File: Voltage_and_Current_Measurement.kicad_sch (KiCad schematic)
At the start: 0 parts

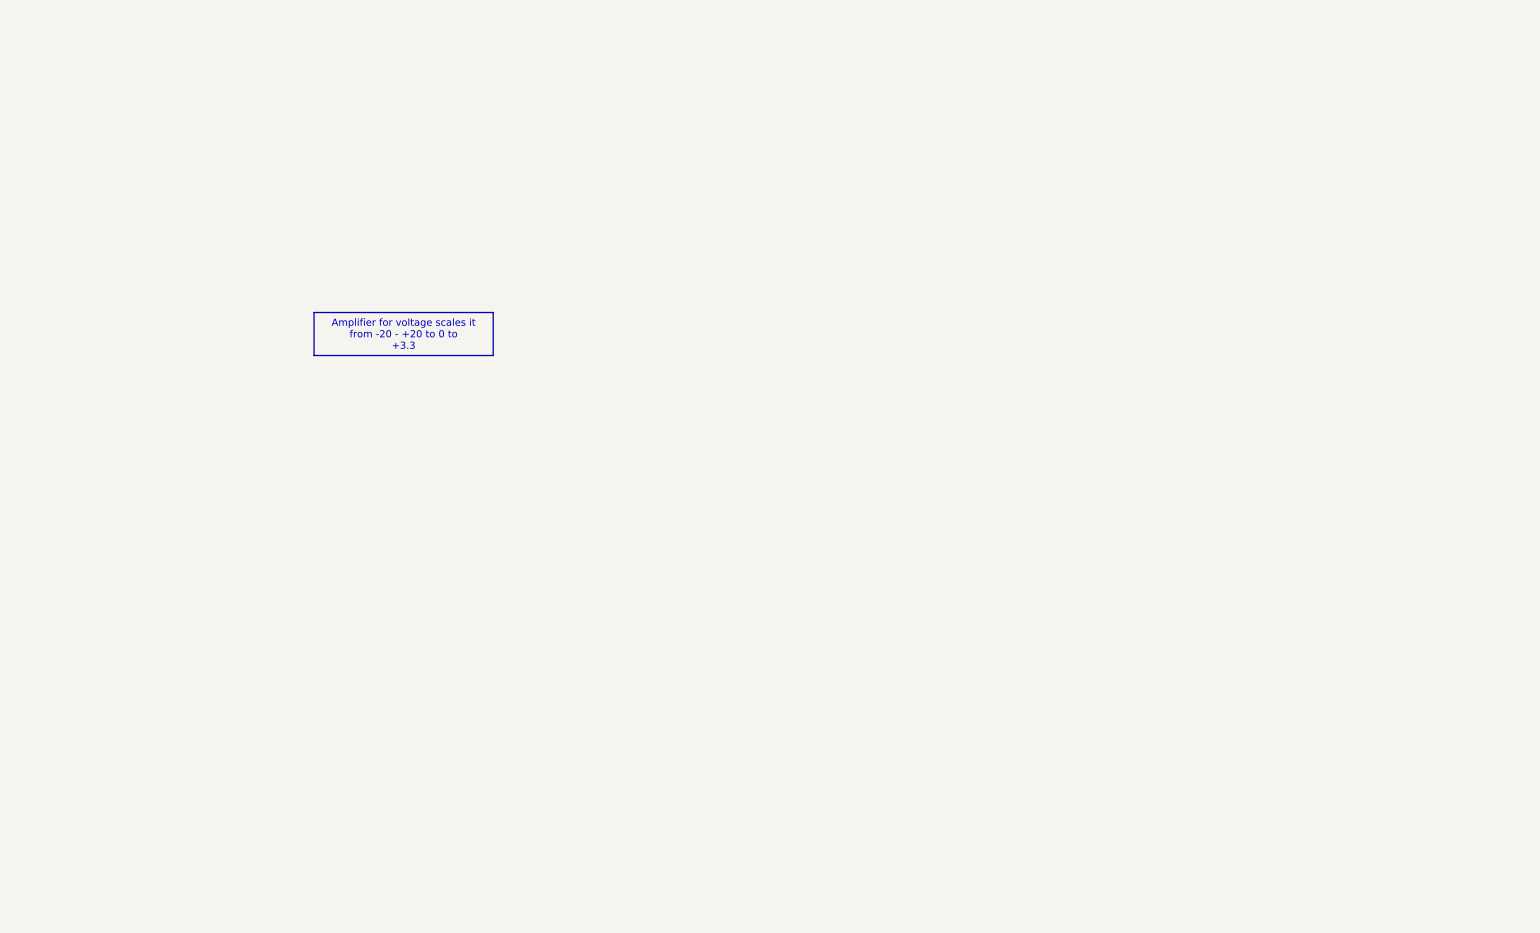
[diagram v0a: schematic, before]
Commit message: added voltage measurement and current measurement
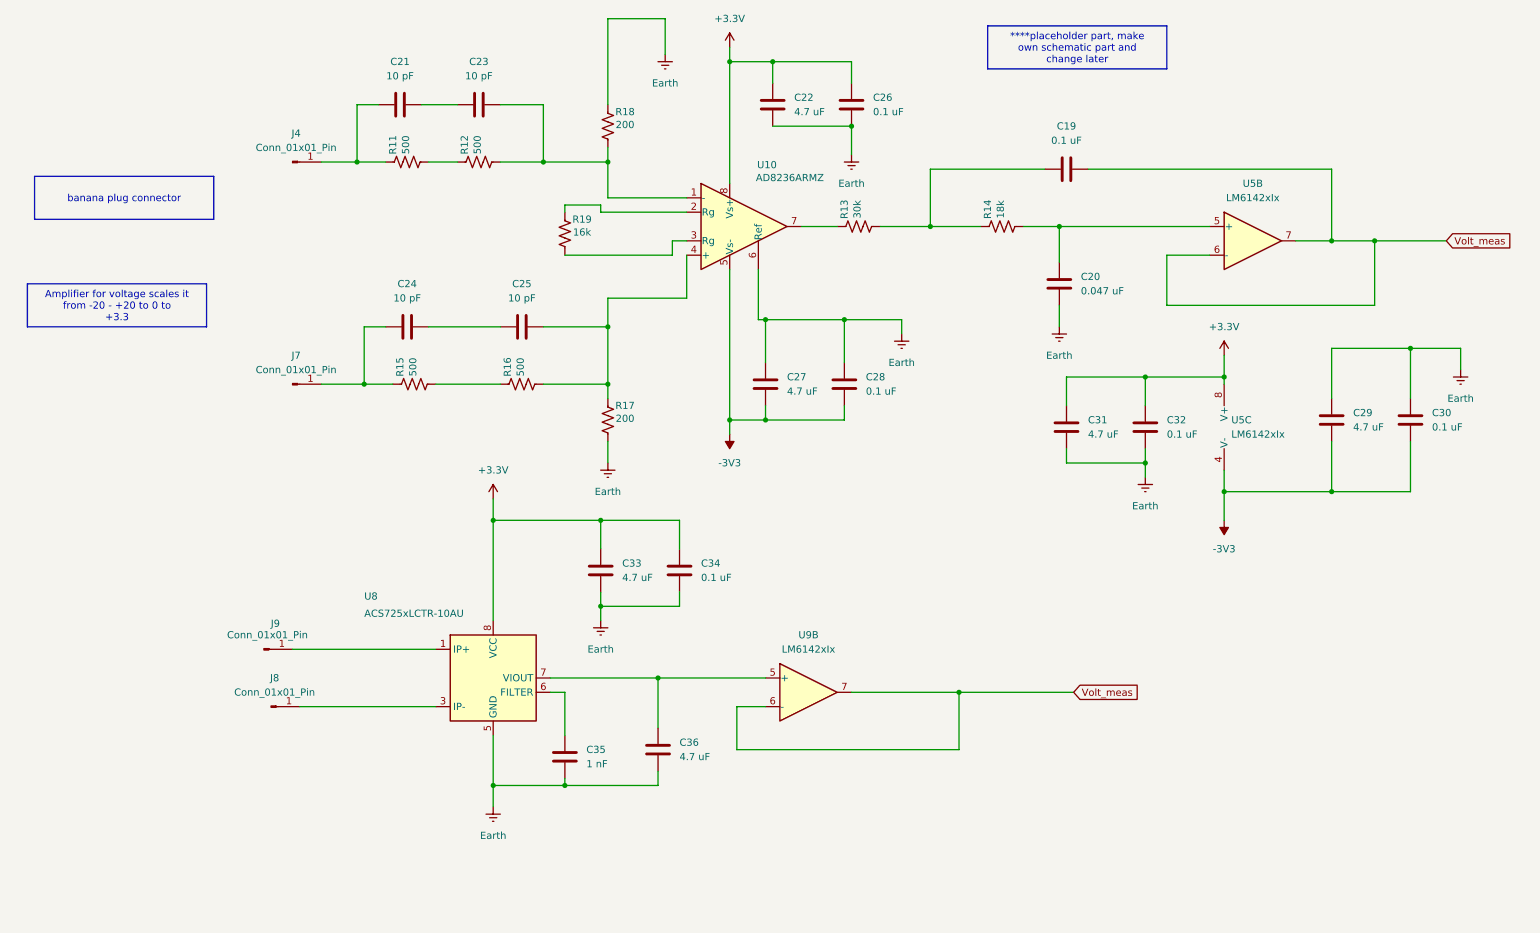
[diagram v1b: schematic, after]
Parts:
- added C19, C26, C28, C30, C32, C34: 0.1 uF, symbol Device:C
- added C20: 0.047 uF, symbol Device:C
- added C21, C23, C24, C25: 10 pF, symbol Device:C
- added C22, C27, C29, C31, C33, C36: 4.7 uF, symbol Device:C
- added C35: 1 nF, symbol Device:C
- added J4, J7, J8, J9: Conn_01x01_Pin, symbol Connector:Conn_01x01_Pin
- added R11, R12, R15, R16: 500, symbol Device:R_US
- added R13: 30k, symbol Device:R_US
- added R14: 18k, symbol Device:R_US
- added R17, R18: 200, symbol Device:R_US
- added R19: 16k, symbol Device:R_US
- added U10: AD8236ARMZ, symbol Amplifier_Instrumentation:AD8236ARMZ
- added U5, U9: LM6142xIx, symbol Amplifier_Operational:LM6142xIx
- added U8: ACS725xLCTR-10AU, Package_SO:SOIC-8_3.9x4.9mm_P1.27mm, symbol Sensor_Current:ACS725xLCTR-10AU
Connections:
- new net: C21.2, C23.1
- new net: C23.2, R12.2, R18.2, U10.1 (-)
- new net: C20.2, R14.2, U5.5 (+)
- new net: R13.1, U10.7
- new net: C19.1, R13.2, R14.1
- new net: C35.2, U8.6 (FILTER)
- new net: C21.1, J4.1 (Pin_1), R11.1
- new net: J9.1 (Pin_1), U8.1 (IP+), U8.2 (IP+)
- new net: J8.1 (Pin_1), U8.3 (IP-), U8.4 (IP-)
- new net: C36.2, U8.7 (VIOUT), U9.5 (+)
- new net: R11.2, R12.1
- new net: R19.1, U10.2 (Rg)
- new net: R19.2, U10.3 (Rg)
- new net: C24.2, C25.1
- new net: C25.2, R16.2, R17.1, U10.4 (+)
- new net: C24.1, J7.1 (Pin_1), R15.1
- new net: R15.2, R16.1
- new net +3.3V: C22.2, C26.2, C31.2, C32.2, C33.2, C34.2, U10.8 (Vs+), U5.8 (V+), U8.8 (VCC)
- new net -3V3: C27.1, C28.1, C29.1, C30.1, U10.5 (Vs-), U5.4 (V-)
- new net Earth: C20.1, C22.1, C26.1, C27.2, C28.2, C29.2, C30.2, C31.1, C32.1, C33.1, C34.1, C35.1, C36.1, R17.2, R18.1, U10.6 (Ref), U8.5 (GND)
- new net Volt_meas: C19.2, U5.6 (-), U5.7, U9.6 (-), U9.7

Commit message: updated schematics added the stm cube project file
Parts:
- removed U5, U9: LM6142xIx, symbol Amplifier_Operational:LM6142xIx
- added U12: LMV324, symbol Amplifier_Operational:LMV324
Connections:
- net +3.3V: now also U12.4 (V+)
- net -3V3: now also U12.11 (V-)
- net Volt_meas: now also U12.1, U12.2 (-)
- net at C20.2, R14.2: now also U12.3 (+)
- net at C36.2, U8.7 (VIOUT): now also U12.5 (+)
- new net Curr_Meas: U12.6 (-), U12.7
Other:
- moved on the sheet: C33, C34, C35, C36, J8, J9, U8

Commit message: changes to schematic and PCB
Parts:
- C19, C20, C21, C22, C23, C24, C25, C26, C27, C28, C29, C30, C31, C32, C33, C34, C35, C36: footprint (none) -> Capacitor_SMD:C_0805_2012Metric
- J4, J7, J8, J9: footprint (none) -> Connector:Banana_Jack_1Pin
- R11, R12, R13, R14, R15, R16, R17, R18, R19: footprint (none) -> Resistor_SMD:R_0805_2012Metric
- U10: footprint (none) -> Package_SO:MSOP-8_3x3mm_P0.65mm
- U12: footprint (none) -> STM32_Play_Board:SOIC-14_3.9x8.7mm_P1.27mm_STM32_Play
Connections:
- net Curr_Meas renamed Curr_meas
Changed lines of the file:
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@@
 		)
 	)
-	(global_label "Curr_Meas"
-		(shape input)
+	(hierarchical_label "Curr_meas"
+		(shape passive)
 		(at 177.8 148.59 0)
 		(fields_autoplaced yes)
@@
 			(justify left)
 		)
-		(property "Intersheetrefs" "${INTERSHEET_REFS}"
-			(at 190.4613 148.59 0)
-			(effects
-				(font
-					(size 1.27 1.27)
-				)
-				(justify left)
-				(hide yes)
-			)
-		)
 	)
-	(global_label "Volt_meas"
-		(shape input)
+	(hierarchical_label "Volt_meas"
+		(shape passive)
 		(at 266.7 54.61 0)
 		(fields_autoplaced yes)
@@
 			(justify left)
 		)
-		(property "Intersheetrefs" "${INTERSHEET_REFS}"
-			(at 279.2403 54.61 0)
-			(effects
-				(font
-					(size 1.27 1.27)
-				)
-				(justify left)
-				(hide yes)
-			)
-		)
 	)
 	(symbol
@@
 			)
 		)
-		(property "Footprint" ""
+		(property "Footprint" "Capacitor_SMD:C_0805_2012Metric"
 			(at 99.06 29.5148 0)
 			(effects
@@
 			)
 		)
-		(property "Footprint" ""
+		(property "Footprint" "Capacitor_SMD:C_0805_2012Metric"
 			(at 197.1548 58.42 0)
 			(effects
@@
 			)
 		)
-		(property "Footprint" ""
+		(property "Footprint" "Resistor_SMD:R_0805_2012Metric"
 			(at 162.814 51.054 90)
 			(effects
@@
 			)
 		)
-		(property "Footprint" ""
+		(property "Footprint" "Capacitor_SMD:C_0805_2012Metric"
 			(at 86.6648 156.21 0)
 			(effects
@@
 			)
 		)
-		(property "Footprint" ""
+		(property "Footprint" "Capacitor_SMD:C_0805_2012Metric"
 			(at 212.3948 83.82 0)
 			(effects
@@
 			)
 		)
-		(property "Footprint" ""
+		(property "Footprint" "STM32_Play_Board:SOIC-14_3.9x8.7mm_P1.27mm_STM32_Play"
 			(at 231.14 52.07 0)
 			(effects
@@
 			)
 		)
-		(property "Footprint" ""
+		(property "Footprint" "Resistor_SMD:R_0805_2012Metric"
 			(at 119.126 34.544 90)
 			(effects
@@
 			)
 		)
-		(property "Footprint" ""
+		(property "Footprint" "Connector:Banana_Jack_1Pin"
 			(at 62.23 40.64 0)
 			(effects
@@
 			)
 		)
-		(property "Footprint" ""
+		(property "Footprint" "Capacitor_SMD:C_0805_2012Metric"
 			(at 259.3848 82.55 0)
 			(effects
@@
 			)
 		)
-		(property "Footprint" ""
+		(property "Footprint" "Resistor_SMD:R_0805_2012Metric"
 			(at 82.804 39.624 90)
 			(effects
@@
 			)
 		)
-		(property "Footprint" ""
+		(property "Footprint" "Resistor_SMD:R_0805_2012Metric"
 			(at 111.506 53.594 90)
 			(effects
@@
 			)
 		)
-		(property "Footprint" ""
+		(property "Footprint" "Capacitor_SMD:C_0805_2012Metric"
 			(at 160.3248 26.67 0)
 			(effects
@@
 			)
 		)
-		(property "Footprint" ""
+		(property "Footprint" "Capacitor_SMD:C_0805_2012Metric"
 			(at 198.4248 83.82 0)
 			(effects
@@
 			)
 		)
-		(property "Footprint" ""
+		(property "Footprint" "Capacitor_SMD:C_0805_2012Metric"
 			(at 85.09 29.5148 0)
 			(effects
@@
 			)
 		)
-		(property "Footprint" ""
+		(property "Footprint" "Resistor_SMD:R_0805_2012Metric"
 			(at 188.214 51.054 90)
 			(effects
@@
 			)
 		)
-		(property "Footprint" ""
+		(property "Footprint" "Capacitor_SMD:C_0805_2012Metric"
 			(at 106.68 68.8848 0)
 			(effects
@@
 			)
 		)
-		(property "Footprint" ""
+		(property "Footprint" "Capacitor_SMD:C_0805_2012Metric"
 			(at 93.0148 123.19 0)
 			(effects
@@
 			)
 		)
-		(property "Footprint" ""
+		(property "Footprint" "Connector:Banana_Jack_1Pin"
 			(at 35.56 151.13 0)
 			(effects
@@
 			)
 		)
-		(property "Footprint" ""
+		(property "Footprint" "Capacitor_SMD:C_0805_2012Metric"
 			(at 103.1748 154.94 0)
 			(effects
@@
 			)
 		)
-		(property "Footprint" ""
+		(property "Footprint" "Capacitor_SMD:C_0805_2012Metric"
 			(at 86.36 68.8848 0)
 			(effects
@@
 			)
 		)
-		(property "Footprint" ""
+		(property "Footprint" "Resistor_SMD:R_0805_2012Metric"
 			(at 84.074 78.994 90)
 			(effects
@@
 			)
 		)
-		(property "Footprint" ""
+		(property "Footprint" "Capacitor_SMD:C_0805_2012Metric"
 			(at 146.3548 26.67 0)
 			(effects
@@
 			)
 		)
-		(property "Footprint" ""
+		(property "Footprint" "Capacitor_SMD:C_0805_2012Metric"
 			(at 245.4148 82.55 0)
 			(effects
@@
 			)
 		)
-		(property "Footprint" ""
+		(property "Footprint" "Connector:Banana_Jack_1Pin"
 			(at 34.29 140.97 0)
 			(effects
@@
 			)
 		)
-		(property "Footprint" ""
+		(property "Footprint" "Resistor_SMD:R_0805_2012Metric"
 			(at 103.124 78.994 90)
 			(effects
@@
 			)
 		)
-		(property "Footprint" ""
+		(property "Footprint" "STM32_Play_Board:SOIC-14_3.9x8.7mm_P1.27mm_STM32_Play"
 			(at 228.6 85.09 0)
 			(effects
@@
 			)
 		)
-		(property "Footprint" ""
+		(property "Footprint" "Capacitor_SMD:C_0805_2012Metric"
 			(at 159.0548 76.2 0)
 			(effects
@@
 			)
 		)
-		(property "Footprint" ""
+		(property "Footprint" "Resistor_SMD:R_0805_2012Metric"
 			(at 119.126 86.614 90)
 			(effects
@@
 			)
 		)
-		(property "Footprint" ""
+		(property "Footprint" "Connector:Banana_Jack_1Pin"
 			(at 62.23 80.01 0)
 			(effects
@@
 			)
 		)
-		(property "Footprint" ""
+		(property "Footprint" "Capacitor_SMD:C_0805_2012Metric"
 			(at 145.0848 76.2 0)
 			(effects
@@
 			)
 		)
-		(property "Footprint" ""
+		(property "Footprint" "STM32_Play_Board:SOIC-14_3.9x8.7mm_P1.27mm_STM32_Play"
 			(at 129.54 146.05 0)
 			(effects
@@
 			)
 		)
-		(property "Footprint" ""
+		(property "Footprint" "Capacitor_SMD:C_0805_2012Metric"
 			(at 203.2 40.9448 0)
 			(effects
@@
 			)
 		)
-		(property "Footprint" ""
+		(property "Footprint" "Resistor_SMD:R_0805_2012Metric"
 			(at 95.504 39.624 90)
 			(effects
@@
 			)
 		)
-		(property "Footprint" ""
+		(property "Footprint" "Package_SO:MSOP-8_3x3mm_P0.65mm"
 			(at 134.62 52.07 0)
 			(effects
@@
 			)
 		)
-		(property "Footprint" ""
+		(property "Footprint" "Capacitor_SMD:C_0805_2012Metric"
 			(at 106.9848 123.19 0)
 			(effects

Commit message: changed schematics
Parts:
- added R25: 10.6k, Resistor_SMD:R_0805_2012Metric, symbol Device:R_US
- added R26: 10k, Resistor_SMD:R_0805_2012Metric, symbol Device:R_US
- R11, R12, R15, R16: value 500 -> 1M
- R17, R18: value 200 -> 10k
- R19: value 16k -> 84.5k
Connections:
- net +3.3V: now also R25.2
- net -3V3: now also C27.2, C28.2; no longer C27.1, C28.1
- net Curr_meas: now also C36.2, U8.7 (VIOUT); no longer U12.6 (-), U12.7
- net Earth: now also C27.1, C28.1, R26.1; no longer C27.2, C28.2, U10.6 (Ref)
- new net: R25.1, R26.2, U12.5 (+)
- new net 1.6 V Ref: U10.6 (Ref), U12.6 (-), U12.7
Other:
- moved on the sheet: C27, C28, U12B
